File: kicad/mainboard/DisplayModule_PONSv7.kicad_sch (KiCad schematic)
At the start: 50 parts, among them J1 Ext. Speaker, J2 54132-4062, J3 2005280040, J4 Micro_SD_Card_Det2, U1 PAM8302AADCR, U2 W25Q128JVS

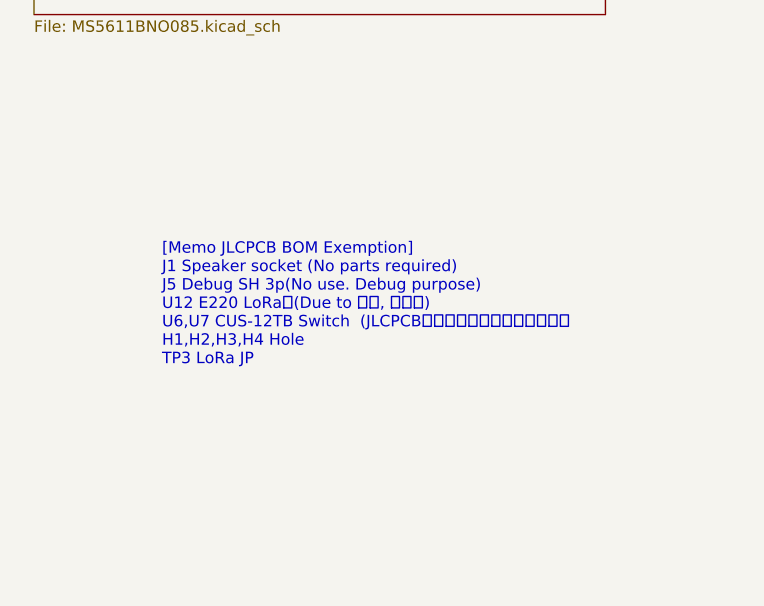
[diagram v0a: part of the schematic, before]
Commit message: 0.962 KiCad 更新、production を git 管理から外す
fabrication-toolkit が生成する production/ は発注のたびに作り直せるうえ、
基板を直すたびに巨大な差分になるので .gitignore に追加した。

Co-Authored-By: Claude Opus 5 <noreply@anthropic.com>
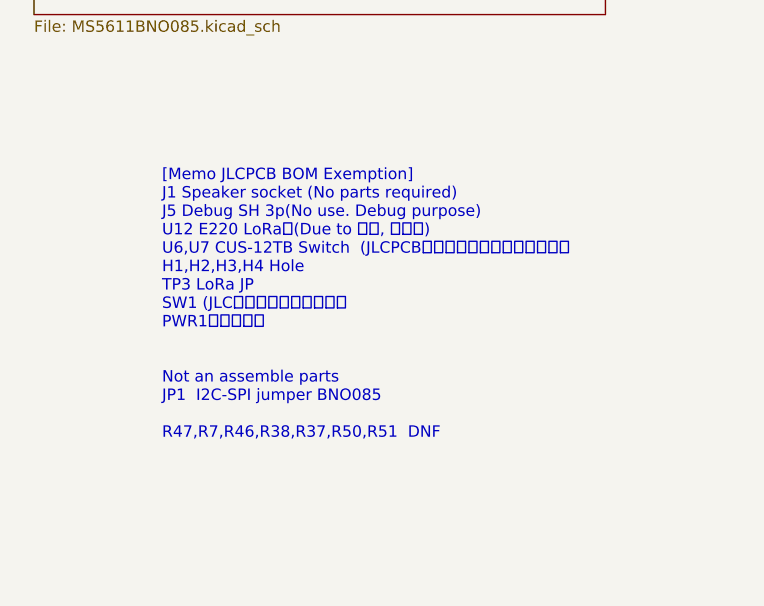
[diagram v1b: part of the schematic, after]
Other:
- note added: "[Memo JLCPCB BOM Exemption] J1 Speaker socket (No parts required) J5 Debug SH 3p(No use. Debug purpose) U12 E220 LoRa (Due to 技適, 手実装) U6,U7 CUS-12TB Switch (JLCPCBにないパーツのため手実装） H1,H2,H3,H4 Hole TP3 LoRa JP SW1 (JLCにないパーツのため） PWR1（コスト） Not an assemble parts JP1 I2C-SPI jumper BNO085 R47,R7,R46,R38,R37,R50,R51 DNF"
- note removed: "[Memo JLCPCB BOM Exemption] J1 Speaker socket (No parts required) J5 Debug SH 3p(No use. Debug purpose) U12 E220 LoRa (Due to 技適, 手実装) U6,U7 CUS-12TB Switch (JLCPCBにないパーツのため手実装） H1,H2,H3,H4 Hole TP3 LoRa JP"
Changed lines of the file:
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@@
 		)
 	)
-	(text "[Memo JLCPCB BOM Exemption]\nJ1 Speaker socket (No parts required)\nJ5 Debug SH 3p(No use. Debug purpose)\nU12 E220 LoRa　(Due to 技適, 手実装)\nU6,U7 CUS-12TB Switch  (JLCPCBにないパーツのため手実装）\nH1,H2,H3,H4 Hole\nTP3 LoRa JP"
+	(text "[Memo JLCPCB BOM Exemption]\nJ1 Speaker socket (No parts required)\nJ5 Debug SH 3p(No use. Debug purpose)\nU12 E220 LoRa　(Due to 技適, 手実装)\nU6,U7 CUS-12TB Switch  (JLCPCBにないパーツのため手実装）\nH1,H2,H3,H4 Hole\nTP3 LoRa JP\nSW1 (JLCにないパーツのため）\nPWR1（コスト）\n\n\nNot an assemble parts\nJP1  I2C-SPI jumper BNO085\n\nR47,R7,R46,R38,R37,R50,R51  DNF"
 		(exclude_from_sim no)
 		(at 232.664 128.778 0)

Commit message: 0.986 新基板（SCH16T 外付け）の kicad を追加し、ガーバー出力を git から外した
kicad/IMU_murata/ — SCH16T-K01-10 のブレイクアウト（新規）
本体の J7（Molex 200528-0080・8pin FPC）へ 1:1 ケーブルで繋ぐ外付け基板。
J1 のピン順を本体 J7 と一致させてある（1=+3V3 2=RESET 3=MOSI 4=CS 5=SCK
6=SYNC 7=MISO 8=GND）。シンボルとフットプリントも同梱。
- ★ R2（CS-GND の 4.7k）は実装しない。CS は負論理なので、プルダウンすると
  MCU が駆動していない間セレクト状態になる。R1（EXTRESN プルアップ）は実装する
- 本体側の GPIO 割り当ては settings.h の SCH16T_PIN_* が正本
  （一覧は docs/imu_sch16t_plan.md §3）

mainboard / GNSS モジュールの更新
- mainboard: DisplayModule_PONSv7 の pcb / pro / sch、MS5611BNO085.kicad_sch、
  SHT_RP2354B.kicad_sch
- GNSS モジュール: pcb / pro / sch、および QRv7 と FPC 4p のフットプリントを
  同プロジェクトの Footprints/ へ取り込み

kicad/FPC/ を畳んだ
FPC コネクタ 1 個のためのプロジェクトだったので、フットプリントを
kicad/GNSSboard_SAM-M10Q/Footprints/ へ移して削除した。
中身は同じで、差分は KiCad が再生成する uuid だけ。

ガーバー・ドリルのプロット出力を git から外した
kicad/.gitignore に追加（*.gbr *.gbl *.gbs *.gbp *.gbo *.gm1 *.gtl *.gts
*.gtp *.gto *.drl と、保険の *plot/ *plot.zip）。発注のたびに作り直せるうえ、
基板を直すたびに巨大な差分になる（ルート .gitignore の production/ と同じ理由）。
★ 入れ物のフォルダ名で書かないこと。v5_1plot/ のような名前は付け方が毎回違うので
  次の基板で外れる。既存の *-backups/ / *.kicad_prl と同じ方針。

Co-Authored-By: Claude Opus 5 <noreply@anthropic.com>
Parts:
- added C39: 10u, GPS_TFT:C_0402_1005Metric_small_pads, symbol Device:C
- added Q2: AO3401A, Package_TO_SOT_SMD:SOT-23, symbol Transistor_FET:AO3401A
- FB1, FB2: value 390 -> 600; footprint Inductor_SMD:L_1206_3216Metric_Pad1.22x1.90mm_HandSolder -> Inductor_SMD:L_0805_2012Metric; LCSC C88995 -> C1017
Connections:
- net +3V3: now also C39.1, Q2.2 (S)
- net GND: now also C39.2
- net PWR_TFT: no longer names the net of R9.1
- net PWR_TFT: now also Q2.3 (D)
- new net TFT_MOSFET_G: Q2.1 (G)
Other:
- note added: "GZ2012D601TF"
- note removed: "BLM31PG391SN1L"

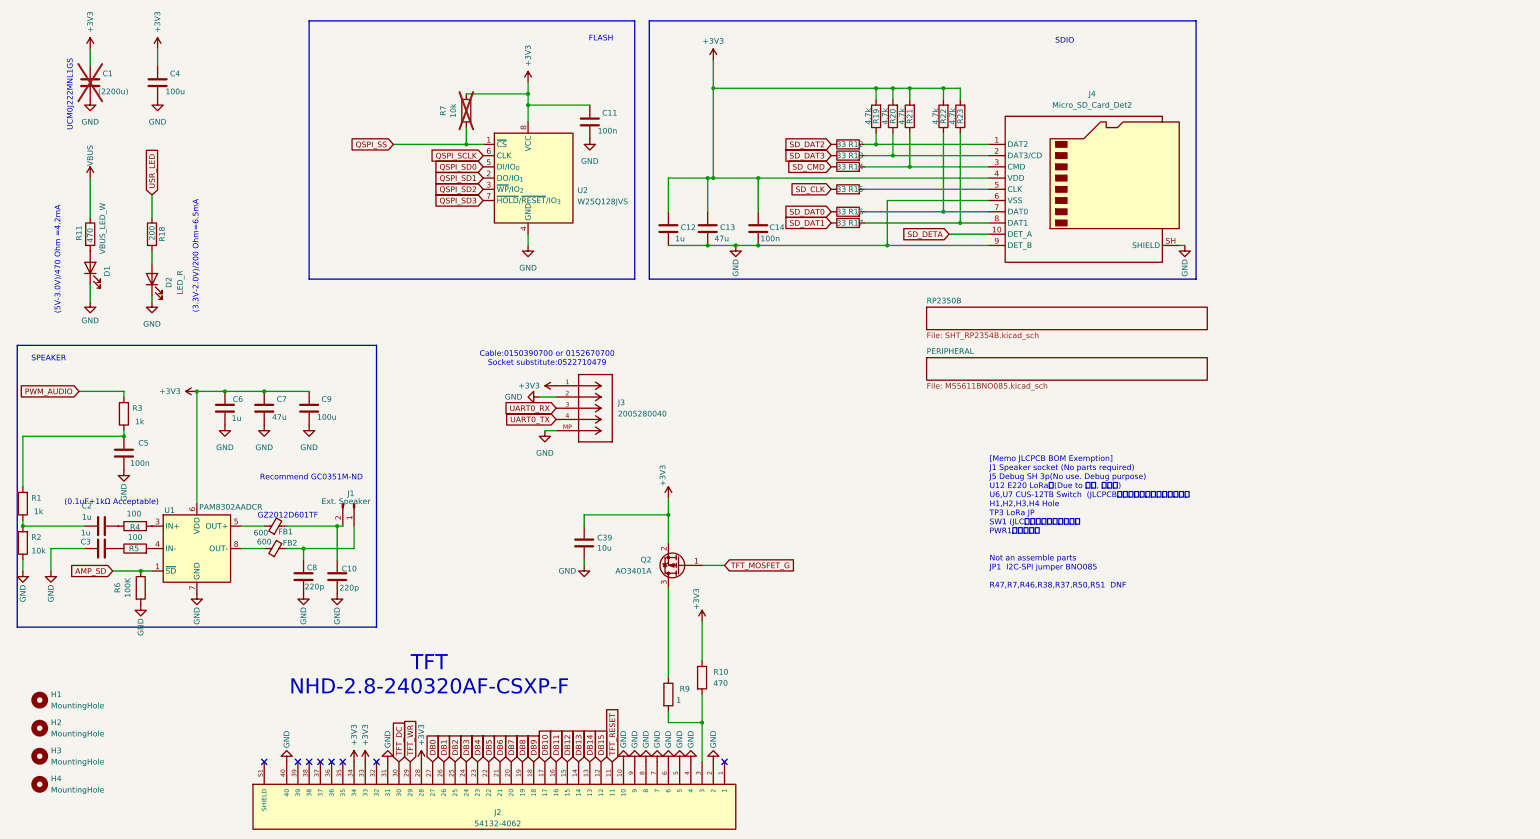
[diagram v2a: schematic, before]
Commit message: 0.993 v7.1 基板の回路図と PCB を仕上げ、SW OFF のままの充電と電源異常を画面と音声で知らせるようにした
- power.cpp（新規）: USB の判定を usb_power_present() に一本化（v7.1 は VBUS を
  GPIO47 の ADC で測る）。電源経路の異常（2026-10-15 の充電 IC 焼損）を検出し、
  地図の POWER FAULT!! と power_fault.wav（30 秒ごと・最低音量 60）で知らせる。
  受信機は LINK_ST_PWR_FAULT を受けてトーン（同じ音声だとボートへの指示に聞こえる）
- v7.1: SW を OFF にしたまま USB で充電していると満充電にならない（Q3 のボディ
  ダイオード経由）。SW4 の OFF 側が GPIO40 を GND に落とすのを読み、地図に注意を出し
  1 度だけ読み上げる（charge_sw_off / charge_sw_on。排他グループ WAV_EXCL_CHARGE_SW）。
  移動中・ミラー中・リプレイ中・デモ中は出さない。判定に USB を入れない
  （VBUS が一瞬 4.3V を割ると 0V が本物の電池電圧として流れるため）。このあいだは
  電池低下の警告を止め、無線は RHAVE_VOLT を立てず LINK_ST_USB_SW_OFF、CSV は空欄
- 受信モードの電池表示を s55r42 の形に。SW OFF のまま USB の側は s5V / r5V
- backlight.cpp（新規）: v7.1 のバックライト PWM と VEML7700 の自動調光。
  飛行 CSV に lux / backlight 列
- E220 の M0/M1 は v7.1 で GPIO31 へ（GPIO47 は USB_SENS）
- 本体の回路図・PCB: SCH16T の J6 を逆順に（完成済みの FPC で J6-n ↔ J3-(9-n)）、
  F1 0805L035 → 0805L050（夏の充電で切れない）、R34/R35 を 10k/5.1k、C32 を 10µF 0805、
  SPI1 の SCK/MOSI/CS に 33Ω（R49〜R51）、スライドスイッチを MST-12D18G2 に、
  回路図とつながらない旧フットプリント（C33/R37/R38/R11 470Ω）を削除、DNP の BOM 除外、
  CUS-12TB の残骸とライブラリ登録を削除、メモの部品番号を v7.1 に
- GNSS 基板を 5 ピン（V_BCKUP）に。バックアップ電池は本体へ移した
- case_cover（照度センサー VEML7700）の kicad を追加。IMU ブレイクアウトの R2 を DNP
- 音声 3 本（power_fault / charge_sw_off / charge_sw_on）は macOS の音声合成の仮音声
- docs/pons_power.md（新規）。README の「自作の手順」を v7.1 に書き直し、
  SCH16T の配線の記述（J7・1:1 ケーブル）を J6・逆順に直した
- gen_wav_flash.py はコメント中の引用符付きの音声名も拾うので、録音前の名前を書かない

PONS_BOARD は V7 と V71 の両方でビルド OK（3,929,776 / 3,923,504 B）/
gen_wav_flash.py --check は 35 ファイル一致 / 本体 PCB の DRC は未配線 0・回路図と一致
（シルクの 6 件はボタンと USB の突起で意図どおり）/ GNSS 基板も未配線 0 / 実機は未確認

Co-Authored-By: Claude Opus 5.5 <noreply@anthropic.com>
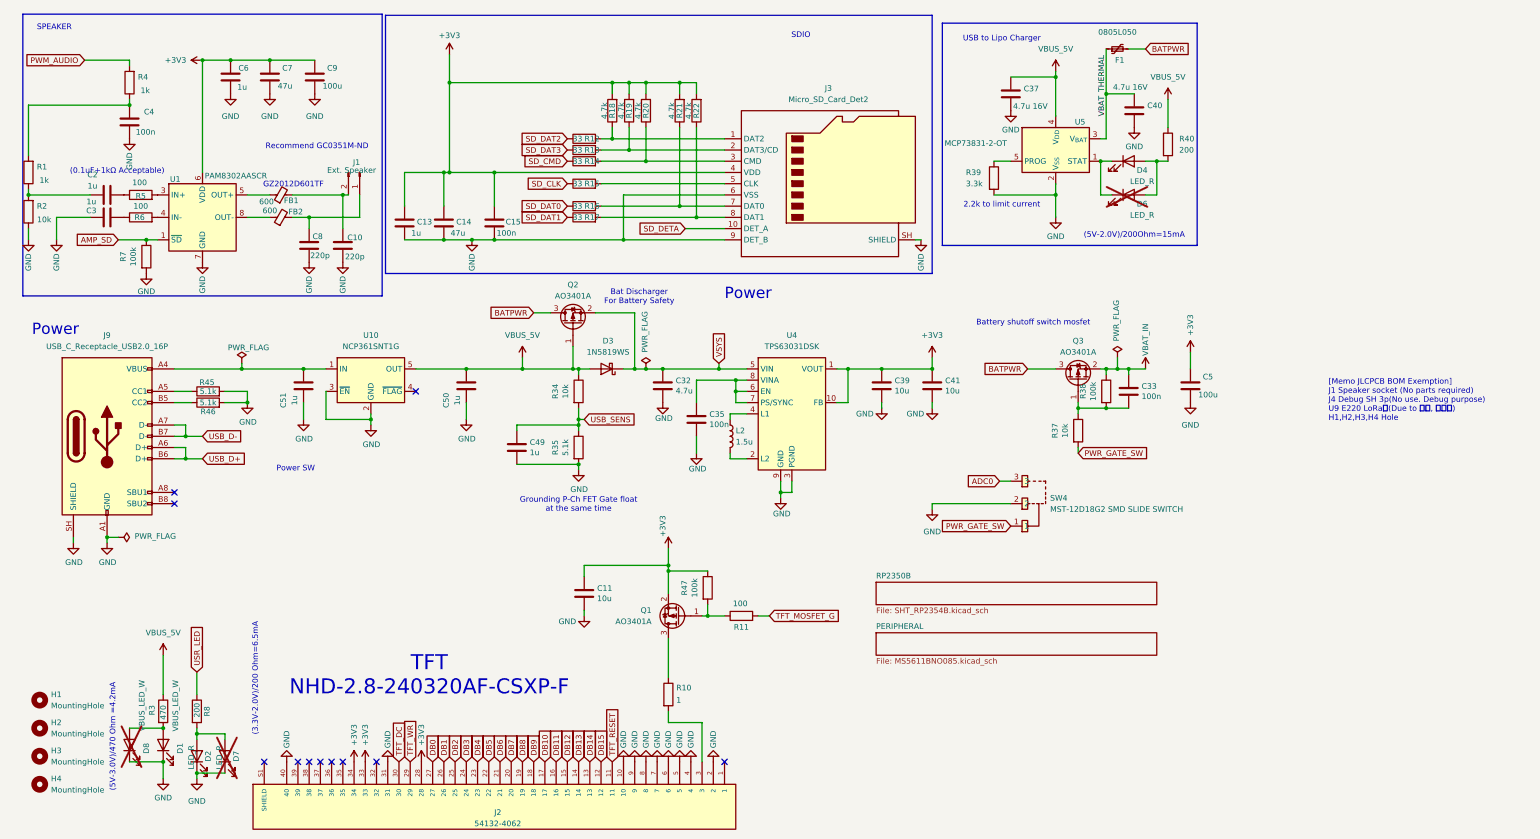
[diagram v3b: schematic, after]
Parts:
- removed C1: (2200u), Capacitor_SMD:CP_Elec_10x10.5, symbol Device:C
- removed C11: 100n, GPS_TFT:C_0402_1005Metric_small_pads, symbol Device:C
- removed C4: 100u, Capacitor_SMD:C_1206_3216Metric, symbol Device:C
- removed J3: 2005280040, Connector_FFC-FPC:Molex_200528-0040_1x04-1MP_P1.00mm_Horizontal, symbol 2005280040:2005280040
- removed R10: 470, Resistor_SMD:R_0402_1005Metric, symbol Device:R
- removed R18: 200, Resistor_SMD:R_0402_1005Metric, symbol Device:R
- removed R7: 10k, Resistor_SMD:R_0603_1608Metric_Pad0.98x0.95mm_HandSolder, symbol Device:R
- removed U2: W25Q128JVS, Package_SO:SOIC-8_5.3x5.3mm_P1.27mm, symbol Memory_Flash:W25Q128JVS
- added C32: 4.7u, GPS_TFT:C_0402_1005Metric_small_pads, symbol Device:C
- added C33, C35: 100n, GPS_TFT:C_0402_1005Metric_small_pads, symbol Device:C
- added C37, C40: 4.7u 16V, Capacitor_SMD:C_0603_1608Metric, symbol Device:C
- added C39, C41: 10u, GPS_TFT:C_0402_1005Metric_small_pads, symbol Device:C
- added C49, C50, C51: 1u, GPS_TFT:C_0402_1005Metric_small_pads, symbol Device:C
- added C5: 100u, Capacitor_SMD:C_1206_3216Metric, symbol Device:C
- added D3: 1N5819WS, Diode_SMD:D_SOD-323, symbol Diode:SS16
- added D4, D6, D7: LED_R, LED_SMD:LED_0603_1608Metric_Pad1.05x0.95mm_HandSolder, symbol Device:LED
- added D8: VBUS_LED_W, LED_SMD:LED_0603_1608Metric_Pad1.05x0.95mm_HandSolder, symbol Device:LED
- added F1: 0805L050, Fuse:Fuse_0805_2012Metric, symbol Device:Polyfuse_Small
- added J9: USB_C_Receptacle_USB2.0_16P, Connector_USB:USB_C_Receptacle_HRO_TYPE-C-31-M-12, symbol Connector:USB_C_Receptacle_USB2.0_16P
- added L2: 1.5u, Inductor_SMD:L_APV_ANR3015, symbol Device:L
- added Q2, Q3: AO3401A, Package_TO_SOT_SMD:SOT-23, symbol dmp2045:DMP2045
- added R3: 470, Resistor_SMD:R_0402_1005Metric, symbol Device:R
- added R34, R37: 10k, Resistor_SMD:R_0402_1005Metric, symbol Device:R
- added R35, R45, R46: 5.1k, Resistor_SMD:R_0402_1005Metric, symbol Device:R
- added R38, R47: 100k, Resistor_SMD:R_0402_1005Metric, symbol Device:R
- added R39: 3.3k, Resistor_SMD:R_0402_1005Metric, symbol Device:R
- added R40, R8: 200, Resistor_SMD:R_0402_1005Metric, symbol Device:R
- added SW4: MST-12D18G2 SMD SLIDE SWITCH, GPS_TFT:SW-SMD_3P-L9.1-W3.5-P2.50_MST-12D18G2, symbol Murata:MST-12D18G2SMDSLIDESWITCH
- added U10: NCP361SNT1G, Package_SO:TSOP-5_1.65x3.05mm_P0.95mm, symbol Power_Protection:NCP361SN
- added U4: TPS63031DSK, Package_SON:WSON-10-1EP_2.5x2.5mm_P0.5mm_EP1.2x2mm, symbol Regulator_Switching:TPS63031DSK
- added U5: MCP73831-2-OT, Package_TO_SOT_SMD:SOT-23-5, symbol Battery_Management:MCP73831-2-OT
- Q1: renamed from Q2; LCSC (none) -> C15127
- R11: value 470 -> 100; LCSC C25117 -> C25076
- R7: renamed from R6; value 100K -> 100k
- U1: value PAM8302AADCR -> PAM8302AASCR; footprint Package_SO:SO-8_3.9x4.9mm_P1.27mm -> Package_SO:MSOP-8_3x3mm_P0.65mm; symbol Amplifier_Audio:PAM8302AAD -> Amplifier_Audio:PAM8302AAS; LCSC C112137 -> C113367
- renumbered C39 to C11, C12 to C13, C13 to C14, C14 to C15, C5 to C4, J4 to J3, R9 to R10, R19 to R18, R20 to R19, R21 to R20, R22 to R21, R23 to R22, R3 to R4, R4 to R5, R5 to R6
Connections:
- net +3V3: now also C39.1, C41.1, C5.1, R47.1, U4.1 (VOUT), U4.10 (FB)
- net GND: now also C32.2, C35.2, C37.2, C39.2, C40.2, C41.2, C49.2, C5.2, C50.1, C51.1, D7.1 (K), D8.1 (K), J9.A1 (GND), J9.A12 (GND), J9.B1 (GND), J9.B12 (GND), J9.SH (SHIELD), R35.2, R39.2, R45.2, R46.2, SW4.2, U10.2 (GND), U10.3 (~{EN}), U4.11 (PGND), U4.3 (PGND), U4.9 (GND), U5.2 (V_{SS})
- net TFT_MOSFET_G: now also R11.2; no longer Q1.1 (G)
- net USR_LED: now also R8.1
- net at D1.2 (A): now also D8.2 (A), R3.2; no longer R11.2
- net at D2.2 (A): now also D7.2 (A), R8.2
- net VBUS: no longer names the net of R11.1
- net VBUS: now also Q1.1 (G), R47.2
- new net: J9.A5 (CC1), R45.1
- new net: D4.1 (K), D6.1 (K), U5.1 (STAT)
- new net: R39.1, U5.5 (PROG)
- new net: J9.B5 (CC2), R46.1
- new net: C51.2, J9.A4 (VBUS), J9.A9 (VBUS), J9.B4 (VBUS), J9.B9 (VBUS), U10.1 (IN)
- new net: D4.2 (A), D6.2 (A), R40.2
- new net: L2.2, U4.2 (L2)
- new net: L2.1, U4.4 (L1)
- new net: C35.1, U4.6 (EN), U4.7 (PS/SYNC), U4.8 (VINA)
- new net: C33.2, Q3.1 (G), R37.1, R38.2
- new net ADC0: SW4.3
- new net BATPWR: F1.2, Q2.3 (D), Q3.3 (D)
- new net PWR_GATE_SW: R37.2, SW4.1
- new net USB_D+: J9.A6 (D+), J9.B6 (D+)
- new net USB_D-: J9.A7 (D-), J9.B7 (D-)
- new net USB_SENS: C49.1, R34.2, R35.1
- new net VBAT_IN: C33.1, Q3.2 (S), R38.1
- new net VBAT_THERMAL: C40.1, F1.1, U5.3 (V_{BAT})
- new net VBUS_5V: C37.1, C50.2, D3.2 (A), Q2.1 (G), R3.1, R34.1, R40.1, U10.5 (OUT), U5.4 (V_{DD})
- new net VSYS: C32.1, D3.1 (K), Q2.2 (S), U4.5 (VIN)
- no-connect marks 8 -> 11
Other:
- note added: "(5V-2.0V)/200Ohm=15mA"
- note added: "2.2k to limit current"
- note added: "Bat Discharger For Battery Safety"
- note added: "Battery shutoff switch mosfet"
- note added: "Grounding P-Ch FET Gate float at the same time"
- note added: "Power"
- note added: "Power SW"
- note added: "USB to Lipo Charger"
- note added: "[Memo JLCPCB BOM Exemption] J1 Speaker socket (No parts required) J4 Debug SH 3p(No use. Debug purpose) U9 E220 LoRa (Due to 技適, 手実装) H1,H2,H3,H4 Hole"
- note removed: "Cable:0150390700 or 0152670700 Socket substitute:0522710479"
- note removed: "FLASH"
- note removed: "UCM0J222MNL1GS"
- note removed: "[Memo JLCPCB BOM Exemption] J1 Speaker socket (No parts required) J5 Debug SH 3p(No use. Debug purpose) U12 E220 LoRa (Due to 技適, 手実装) U6,U7 CUS-12TB Switch (JLCPCBにないパーツのため手実装） H1,H2,H3,H4 Hole TP3 LoRa JP SW1 (JLCにないパーツのため） PWR1（コスト） Not an assemble parts JP1 I2C-SPI jumper BNO085 R47,R7,R46,R38,R37,R50,R51 DNF"
- moved on the sheet: C10, C11, C13, C14, C15, C2, C3, C4, C6, C7, C8, C9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

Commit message: 0.994 GNSS の翌日起動を速くし、本番前チェック・高温充電の警告・電池低下の点滅を入れ、v7.1 基板の逆接保護と発注前の修正を仕上げた
- GNSS: AssistNow Autonomous を有効化（CFG-VALSET で RAM と BBR。settings.h の
  GNSS_USE_ANA。0 でも OFF を書き込む＝BBR に残った ON を消すため）。前日と同じ時間帯の
  起動が 23〜28 秒 → 3〜4 秒（BT1 が生きていること）。NAV-AOPSTATUS を 1Hz で受け、
  GNSS DETAIL 3 に ANA:ON data/use/calc、log.txt に「... after boot」（TTFF）・最初の
  測位の軌道の出どころ・10 分ごとの計算時間。ACK 待ちの間も imu_service_if_due() を
  呼ぶ（以前からの抜け）
- readiness.cpp（新規）: 本番前チェック。GNSS・IMU・ESKF・較正（マウント外れだけ。
  日付またぎは推測なので入れない＝台の上での APPLY を促さない）・地上の姿勢・設定画面の
  赤丸・USB・電池 50%・SD・無線（送信モード）がそろい、地上で止まっていたら 1 度だけ
  「準備完了」（ready.wav）。欠けていれば設定画面の右上に項目名。受信モード・リプレイ・
  デモは対象外。既存の判定を読むだけで、条件は書き写さない
- 高温での充電の警告（v7・v7.1）: USB 接続中に MS5611 が 45°C を 30 秒超え続けたら
  地図に TOO HOT TO CHARGE と charge_hot.wav（60 秒ごと・最低音量 60）。電池の仕様は
  充電 0〜45°C。地図の段は電源異常と共用（異常 ＞ 高温 ＞ SW OFF）
- 電池低下のときの点滅（v7.1）: 電池低下の警告と同じ 3.5V でバックライトを 2 秒点灯・
  4 秒消灯。3.65V か USB で戻る（3.5V で戻すと入り切りをくり返す）。消灯中も本来の
  明るさは追い続ける（照度追従の立ち上がりで 2 秒の点灯が暗くならないように）
- 本体の回路図・PCB: 電池の逆接保護 Q4（AO3401A、D が電池側）＋ R52、PWR1 の
  ネットを VBAT_RAW に。C32 を 10µF 0805 に（10/20 に直したのが 0402 に戻っていた）。
  D5 を RB751S40（逆流が少ない。PCBA で実装）に。古いメモを整理
- IMU 基板の GND が IC1.16・C3 だけ分かれていたのをつないだ。J3 の値を 01x08 に。
  case_cover の部品番号を回路図と一致。GNSS 基板の裏面を GND ベタに（浮いていた
  19 個のビアがつながった）
- 音声 2 本（ready / charge_hot）は macOS の音声合成の仮音声
- docs: pons_power.md に Q4・P-ch FET 3 段の役割・電池の保護回路（DTP603048(PHR) の
  仕様書）・R39 を 2.2kΩ に戻さない理由（電池の最大充電 430mA も超える）・高温の警告・
  電池低下の点滅。README に GNSS の起動・本番前チェック・新しい警報・v7.1 の USB-C と
  充電時間、古い記述（v7 の実結線試験・無線の立ち上げ手順書の冒頭）を今の状態に。
  CLAUDE.md に BBR に書いた GNSS 設定が残る件と readiness.cpp
- kicad/.gitignore に *.pos

PONS_BOARD は V7 と V71 の両方でビルド OK（4,052,376 / 4,046,728 B）/
gen_wav_flash.py --check は 37 ファイル一致 / 本体 PCB の DRC は未配線 0・回路図と一致
（シルクの 6 件は意図どおり）/ IMU・カバー・GNSS 基板も未配線 0・回路図と一致 /
BOM の LCSC 番号は全 48 種類を JLC/LCSC の部品情報と照合 / 実機は未確認

Co-Authored-By: Claude Opus 5.5 <noreply@anthropic.com>
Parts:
- removed C5: 100u, Capacitor_SMD:C_1206_3216Metric, symbol Device:C
- added PWR1: 1s Lipo Power input, Connector_JST:JST_PH_S2B-PH-K_1x02_P2.00mm_Horizontal, symbol Connector:Conn_01x02_Pin
- added Q4: AO3401A, Package_TO_SOT_SMD:SOT-23, symbol dmp2045:DMP2045
- added R52: 100k, Resistor_SMD:R_0402_1005Metric, symbol Device:R
- C32: value 4.7u -> 10u; footprint GPS_TFT:C_0402_1005Metric_small_pads -> Capacitor_SMD:C_0805_2012Metric; LCSC C23733 -> C15850
- J2: FT Position Offset (none) -> 0,-1.5; MANUFACTURER Molex -> (none); Manufacturer (none) -> Molex
- U10: FT Rotation Offset (none) -> 90
- U5: FT Rotation Offset (none) -> -90
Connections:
- net GND: now also PWR1.2 (Pin_2), R52.1
- net VBAT_IN: now also Q4.2 (S)
- new net: Q4.1 (G), R52.2
- new net VBAT_RAW: PWR1.1 (Pin_1), Q4.3 (D)
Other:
- note added: "BAT IN"
- note added: "Lipo Charger"
- note added: "Q2: Bat Discharger For Battery Safety"
- note added: "Q3: ユーザー電源スイッチ"
- note added: "Q4: 電池の逆接保護（D が電池側） USB を挿したままの逆接は守れない"
- note added: "USB surge protection."
- note removed: "Bat Discharger For Battery Safety"
- note removed: "Battery shutoff switch mosfet"
- note removed: "Power SW"
- note removed: "USB to Lipo Charger"
- title: PONS for HPA v7 -> PONS for HPA
- moved on the sheet: C10, C2, C3, C32, C33, C35, C39, C4, C41, C49, C50, C51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
